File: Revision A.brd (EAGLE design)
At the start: 152.4 x 101.6 mm, 52 parts, among them IC1 7805T, J1 POWER_JACKPTH, Q1 IRF9530, Q2 IRF9530, Q3 IRF9530, T1 BC547, T2 BC547, T3 BC547, U1 TLV2372IP, U2 LCD-16X2SILK

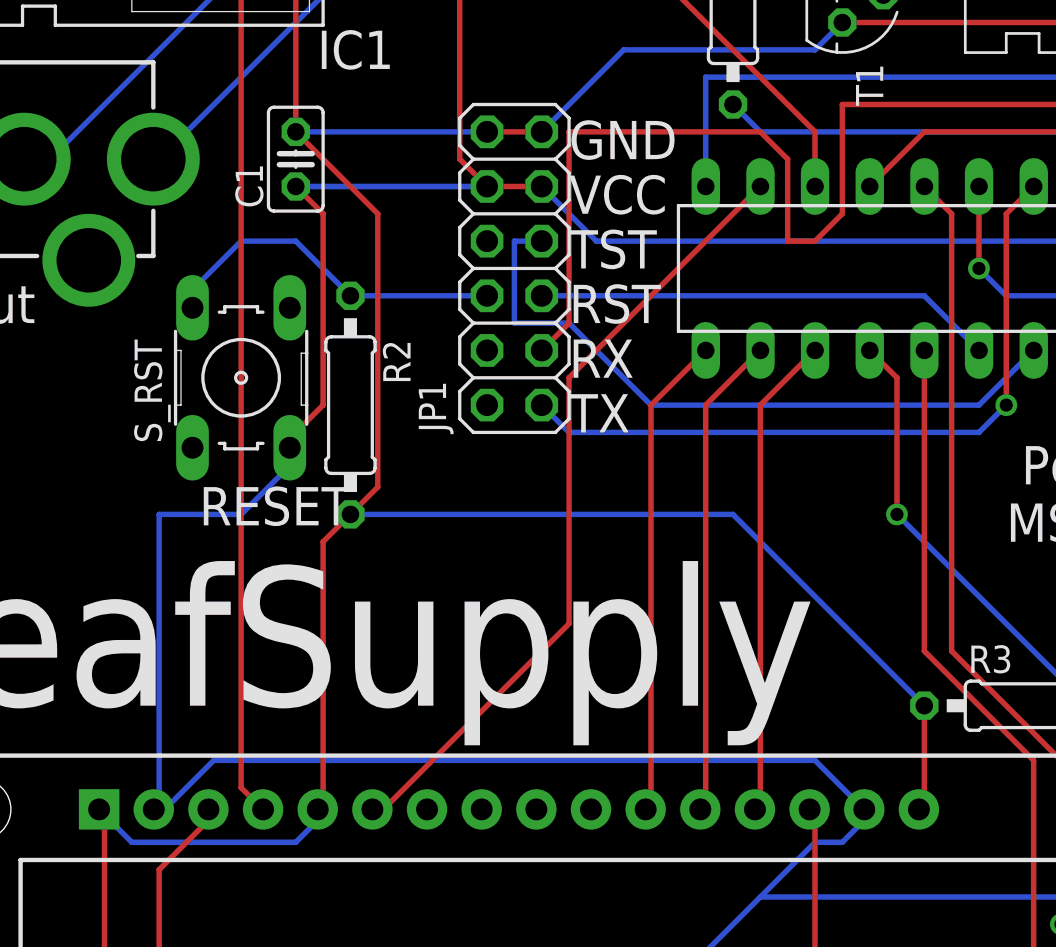
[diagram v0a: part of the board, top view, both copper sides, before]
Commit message: Fixed the RESET pin connection
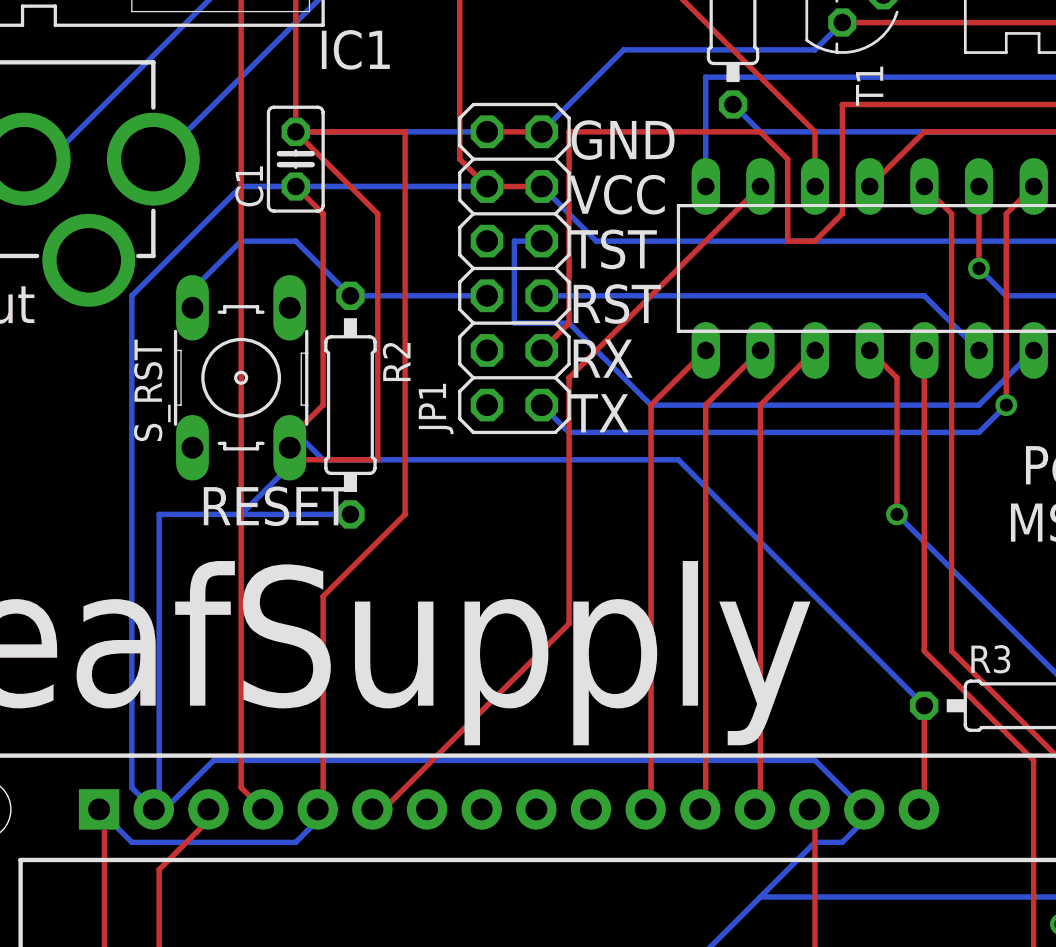
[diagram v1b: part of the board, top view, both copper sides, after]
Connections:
- net +5V: now also R2.2; no longer S_RST.3
- net GND: now also S_RST.3; no longer R2.2
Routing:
- net +5V: track 309.1 -> 347.1 mm
- net GND: track 521.3 -> 551.4 mm
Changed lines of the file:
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@@
 <contactref element="JP1" pad="9"/>
 <contactref element="JP1" pad="10"/>
-<contactref element="S_RST" pad="3"/>
 <contactref element="R1" pad="1"/>
 <contactref element="U2" pad="2"/>
@@
 <wire x1="21.59" y1="78.74" x2="21.59" y2="69.85" width="0.254" layer="1"/>
 <wire x1="20.32" y1="80.01" x2="21.59" y2="78.74" width="0.254" layer="1"/>
-<wire x1="20.32" y1="68.58" x2="20.0406" y2="67.8688" width="0.254" layer="1"/>
 <wire x1="27.94" y1="91.44" x2="24.13" y2="95.25" width="0.254" layer="1"/>
 <wire x1="27.94" y1="81.28" x2="27.94" y2="91.44" width="0.254" layer="1"/>
@@
 <wire x1="17.78" y1="64.77" x2="13.97" y2="64.77" width="0.254" layer="16"/>
 <wire x1="20.32" y1="67.31" x2="17.78" y2="64.77" width="0.254" layer="16"/>
-<wire x1="20.32" y1="67.31" x2="20.0406" y2="67.8688" width="0.254" layer="16"/>
 <wire x1="29.21" y1="80.01" x2="31.75" y2="80.01" width="0.254" layer="1"/>
 <wire x1="92.71" y1="46.99" x2="90.17" y2="44.45" width="0.254" layer="16"/>
@@
 <wire x1="44.45" y1="53.34" x2="16.51" y2="53.34" width="0.254" layer="16"/>
 <wire x1="46.99" y1="50.8" x2="44.45" y2="53.34" width="0.254" layer="16"/>
+<wire x1="46.99" y1="50.8" x2="46.74" y2="51.06" width="0.254" layer="16"/>
+<contactref element="R2" pad="2"/>
+<wire x1="17.78" y1="64.77" x2="22.86" y2="64.77" width="0.254" layer="16"/>
+<wire x1="12.7" y1="52.07" x2="13.97" y2="50.8" width="0.254" layer="16"/>
+<wire x1="12.7" y1="74.93" x2="12.7" y2="52.07" width="0.254" layer="16"/>
+<wire x1="17.78" y1="80.01" x2="12.7" y2="74.93" width="0.254" layer="16"/>
+<wire x1="20.32" y1="80.01" x2="17.78" y2="80.01" width="0.254" layer="16"/>
 <wire x1="13.97" y1="50.8" x2="13.72" y2="51.06" width="0.254" layer="16"/>
-<wire x1="46.99" y1="50.8" x2="46.74" y2="51.06" width="0.254" layer="16"/>
 </signal>
 <signal name="GND">
@@
 <contactref element="JP1" pad="11"/>
 <contactref element="JP1" pad="12"/>
-<contactref element="R2" pad="2"/>
 <contactref element="U2" pad="1"/>
 <contactref element="R1" pad="3"/>
@@
 <wire x1="49.53" y1="50.8" x2="49.53" y2="55.88" width="0.254" layer="1"/>
 <wire x1="49.53" y1="50.8" x2="49.28" y2="51.06" width="0.254" layer="1"/>
-<wire x1="21.59" y1="63.5" x2="22.86" y2="64.77" width="0.254" layer="1"/>
-<wire x1="21.59" y1="50.8" x2="21.59" y2="63.5" width="0.254" layer="1"/>
+<wire x1="21.59" y1="50.8" x2="21.59" y2="60.96" width="0.254" layer="1"/>
 <wire x1="21.59" y1="50.8" x2="21.34" y2="51.06" width="0.254" layer="1"/>
-<wire x1="40.64" y1="64.77" x2="49.53" y2="55.88" width="0.254" layer="16"/>
-<wire x1="22.86" y1="64.77" x2="40.64" y2="64.77" width="0.254" layer="16"/>
+<wire x1="38.1" y1="67.31" x2="49.53" y2="55.88" width="0.254" layer="16"/>
 <wire x1="11.43" y1="11.43" x2="10.16" y2="10.16" width="0.254" layer="1"/>
 <wire x1="11.43" y1="50.8" x2="11.43" y2="11.43" width="0.254" layer="1"/>
@@
 <wire x1="11.43" y1="50.8" x2="11.18" y2="51.06" width="0.254" layer="16"/>
 <wire x1="24.13" y1="78.74" x2="20.32" y2="82.55" width="0.254" layer="1"/>
-<wire x1="24.13" y1="66.04" x2="24.13" y2="78.74" width="0.254" layer="1"/>
-<wire x1="22.86" y1="64.77" x2="24.13" y2="66.04" width="0.254" layer="1"/>
+<wire x1="24.13" y1="67.31" x2="24.13" y2="78.74" width="0.254" layer="1"/>
 <wire x1="135.89" y1="35.56" x2="144.78" y2="44.45" width="0.254" layer="1"/>
 <wire x1="135.89" y1="35.56" x2="135.89" y2="27.94" width="0.254" layer="1"/>
@@
 <wire x1="62.23" y1="72.39" x2="62.23" y2="73.66" width="0.254" layer="1"/>
 <wire x1="62.23" y1="72.39" x2="62.235" y2="72.39" width="0.254" layer="1"/>
+<contactref element="S_RST" pad="3"/>
+<wire x1="24.13" y1="67.31" x2="20.32" y2="67.31" width="0.254" layer="1"/>
+<wire x1="20.32" y1="67.31" x2="20.0406" y2="67.8688" width="0.254" layer="1"/>
+<wire x1="25.4" y1="82.55" x2="20.32" y2="82.55" width="0.254" layer="1"/>
+<wire x1="25.4" y1="64.77" x2="25.4" y2="82.55" width="0.254" layer="1"/>
+<wire x1="21.59" y1="60.96" x2="25.4" y2="64.77" width="0.254" layer="1"/>
+<wire x1="21.59" y1="67.31" x2="38.1" y2="67.31" width="0.254" layer="16"/>
+<wire x1="20.32" y1="68.58" x2="21.59" y2="67.31" width="0.254" layer="16"/>
+<wire x1="20.32" y1="68.58" x2="20.0406" y2="67.8688" width="0.254" layer="16"/>
 </signal>
 <signal name="INT">

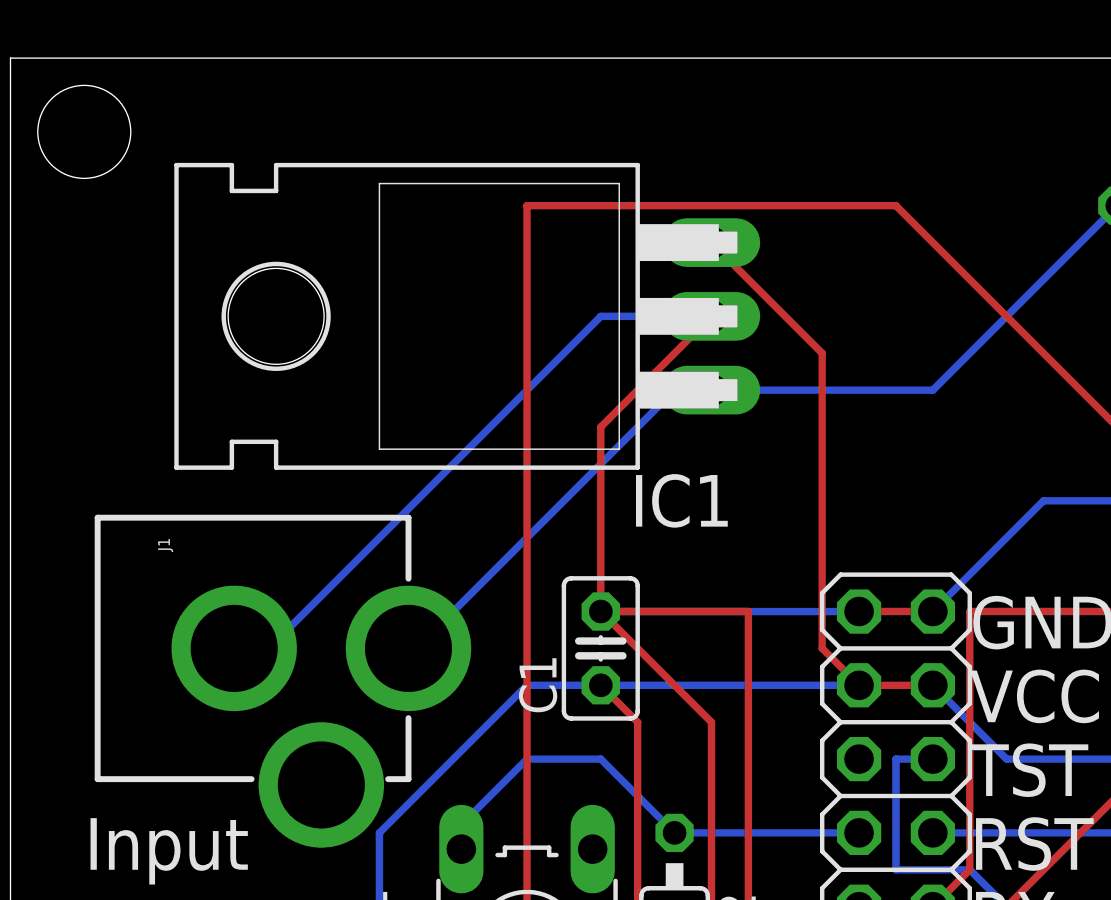
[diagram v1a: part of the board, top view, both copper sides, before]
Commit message: Fixed the voltage regulator for the MCU
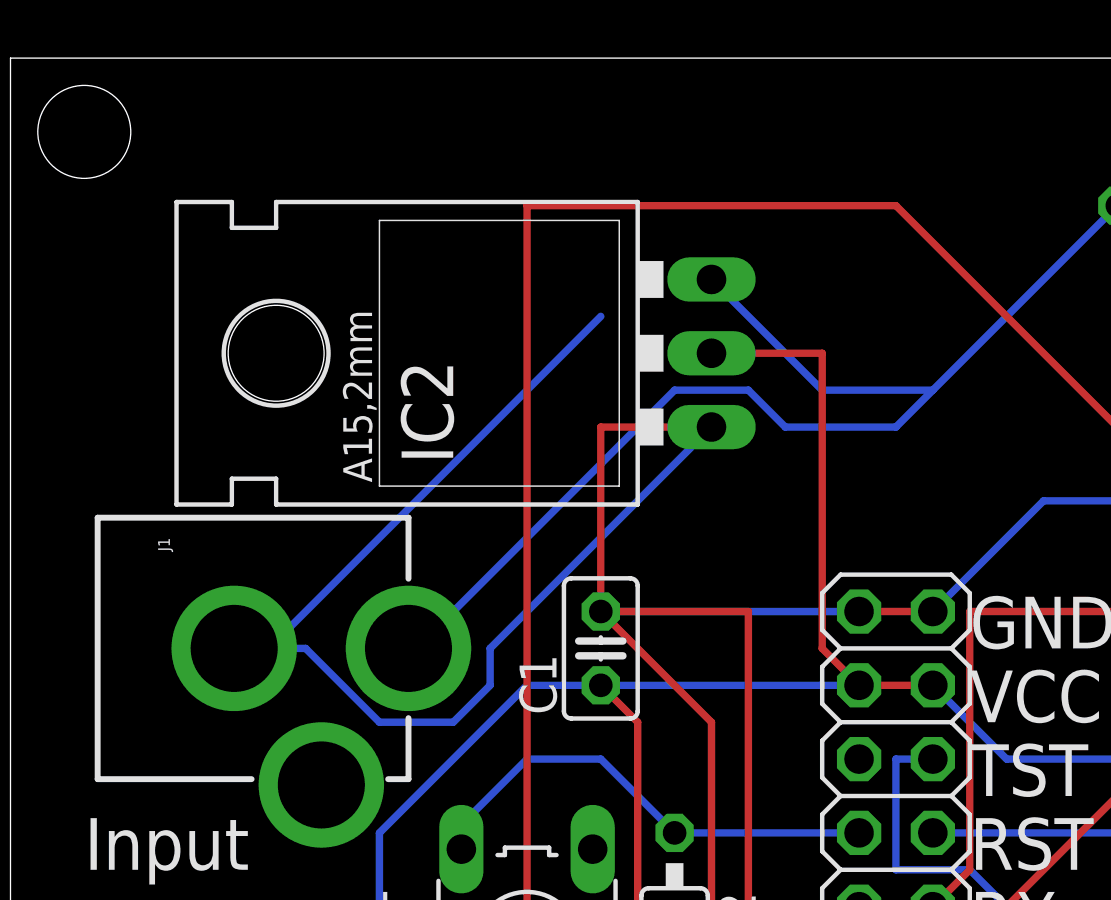
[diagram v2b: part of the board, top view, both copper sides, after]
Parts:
- removed IC1: 7805T, linear:TO220H
- added IC2: LD117AV33, v-reg:TO220L1
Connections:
- net +5V: now also IC2.2; no longer IC1.3
- net GND: now also IC2.1; no longer IC1.2
- net VIN: now also IC2.3; no longer IC1.1
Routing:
- net GND: track 551.4 -> 567.3 mm
- net VIN: track 205.2 -> 215.4 mm
- net +5V: track 347.1 -> 345.6 mm
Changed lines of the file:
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@@
 <elements>
 <element name="U$1" library="TI_MSP430_v16" package="N20" value="G2XX3---N20" x="50.8" y="76.2" rot="R180"/>
-<element name="IC1" library="linear" package="TO220H" value="7805T" x="13.97" y="92.71" rot="R90"/>
 <element name="JP1" library="pinhead" package="2X06" value="" x="30.48" y="76.2" rot="R90"/>
 <element name="C1" library="rcl" package="C025-025X050" value="0.1uF" x="20.32" y="81.28" rot="R90"/>
@@
 <element name="RE1" library="Custom Stuff" package="ECW1J-B" value="ECW1J-B24-BCCO24LECW1J-B" x="99.06" y="10.16"/>
 <element name="J1" library="SparkFun-Connectors" package="POWER_JACK_PTH" value="POWER_JACKPTH" x="0" y="81.28" rot="R270"/>
+<element name="IC2" library="v-reg" package="TO220L1" value="LD117AV33" x="20.32" y="91.44" rot="R90"/>
 </elements>
 <signals>
@@
 <contactref element="U$1" pad="1"/>
 <contactref element="C1" pad="1"/>
-<contactref element="IC1" pad="3"/>
 <contactref element="JP1" pad="9"/>
 <contactref element="JP1" pad="10"/>
@@
 <wire x1="21.59" y1="78.74" x2="21.59" y2="69.85" width="0.254" layer="1"/>
 <wire x1="20.32" y1="80.01" x2="21.59" y2="78.74" width="0.254" layer="1"/>
-<wire x1="27.94" y1="91.44" x2="24.13" y2="95.25" width="0.254" layer="1"/>
 <wire x1="27.94" y1="81.28" x2="27.94" y2="91.44" width="0.254" layer="1"/>
 <wire x1="29.21" y1="80.01" x2="27.94" y2="81.28" width="0.254" layer="1"/>
@@
 <wire x1="20.32" y1="80.01" x2="17.78" y2="80.01" width="0.254" layer="16"/>
 <wire x1="13.97" y1="50.8" x2="13.72" y2="51.06" width="0.254" layer="16"/>
+<contactref element="IC2" pad="2"/>
+<wire x1="27.94" y1="91.44" x2="24.13" y2="91.44" width="0.254" layer="1"/>
 </signal>
 <signal name="GND">
 <contactref element="U$1" pad="20"/>
 <contactref element="C1" pad="2"/>
-<contactref element="IC1" pad="2"/>
 <contactref element="JP1" pad="11"/>
 <contactref element="JP1" pad="12"/>
@@
 <wire x1="31.75" y1="82.55" x2="35.56" y2="86.36" width="0.254" layer="16"/>
 <wire x1="29.21" y1="82.55" x2="20.32" y2="82.55" width="0.254" layer="16"/>
-<wire x1="20.32" y1="88.9" x2="24.13" y2="92.71" width="0.254" layer="1"/>
 <wire x1="20.32" y1="82.55" x2="20.32" y2="88.9" width="0.254" layer="1"/>
 <wire x1="20.32" y1="92.71" x2="8.89" y2="81.28" width="0.254" layer="16"/>
-<wire x1="24.13" y1="92.71" x2="20.32" y2="92.71" width="0.254" layer="16"/>
-<wire x1="8.89" y1="81.28" x2="7.7" y2="81.28" width="0.254" layer="16"/>
 <wire x1="29.21" y1="82.55" x2="31.75" y2="82.55" width="0.254" layer="1"/>
 <wire x1="49.53" y1="50.8" x2="49.53" y2="55.88" width="0.254" layer="1"/>
@@
 <wire x1="20.32" y1="68.58" x2="21.59" y2="67.31" width="0.254" layer="16"/>
 <wire x1="20.32" y1="68.58" x2="20.0406" y2="67.8688" width="0.254" layer="16"/>
+<contactref element="IC2" pad="1"/>
+<wire x1="20.32" y1="88.9" x2="24.13" y2="88.9" width="0.254" layer="1"/>
+<wire x1="16.51" y1="81.28" x2="24.13" y2="88.9" width="0.254" layer="16"/>
+<wire x1="16.51" y1="80.01" x2="16.51" y2="81.28" width="0.254" layer="16"/>
+<wire x1="15.24" y1="78.74" x2="16.51" y2="80.01" width="0.254" layer="16"/>
+<wire x1="12.7" y1="78.74" x2="15.24" y2="78.74" width="0.254" layer="16"/>
+<wire x1="10.16" y1="81.28" x2="12.7" y2="78.74" width="0.254" layer="16"/>
+<wire x1="8.89" y1="81.28" x2="10.16" y2="81.28" width="0.254" layer="16"/>
+<wire x1="8.89" y1="81.28" x2="7.7" y2="81.28" width="0.254" layer="16"/>
 </signal>
 <signal name="INT">
@@
 </signal>
 <signal name="VIN">
-<contactref element="IC1" pad="1"/>
 <contactref element="U1" pad="8"/>
 <contactref element="C9" pad="1"/>
@@
 <contactref element="J1" pad="PWR"/>
 <wire x1="31.75" y1="90.17" x2="38.1" y2="96.52" width="0.254" layer="16"/>
-<wire x1="24.13" y1="90.17" x2="31.75" y2="90.17" width="0.254" layer="16"/>
 <wire x1="22.86" y1="90.17" x2="13.97" y2="81.28" width="0.254" layer="16"/>
-<wire x1="24.13" y1="90.17" x2="22.86" y2="90.17" width="0.254" layer="16"/>
 <wire x1="13.97" y1="81.28" x2="13.7" y2="81.28" width="0.254" layer="16"/>
 <wire x1="116.84" y1="17.78" x2="127" y2="17.78" width="0.254" layer="1"/>
@@
 <wire x1="68.58" y1="97.79" x2="39.37" y2="97.79" width="0.254" layer="16"/>
 <wire x1="72.39" y1="93.98" x2="68.58" y2="97.79" width="0.254" layer="16"/>
+<contactref element="IC2" pad="3"/>
+<wire x1="27.94" y1="90.17" x2="24.13" y2="93.98" width="0.254" layer="16"/>
+<wire x1="31.75" y1="90.17" x2="27.94" y2="90.17" width="0.254" layer="16"/>
+<wire x1="30.48" y1="88.9" x2="31.75" y2="90.17" width="0.254" layer="16"/>
+<wire x1="26.67" y1="88.9" x2="30.48" y2="88.9" width="0.254" layer="16"/>
+<wire x1="25.4" y1="90.17" x2="26.67" y2="88.9" width="0.254" layer="16"/>
+<wire x1="22.86" y1="90.17" x2="25.4" y2="90.17" width="0.254" layer="16"/>
 </signal>
 <signal name="DATA">
